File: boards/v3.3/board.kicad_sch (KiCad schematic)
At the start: 50 parts, among them J1 KF301-2P, J2 KF301-2P, J3 KF301-2P, J4 KF301-2P, J5 KF301-2P, J6 KF301-2P, P1 Pin Header, P2 Pin Header, P3 Pin Header, P4 Pin Header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

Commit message: The last board and documentation update
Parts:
- added AMP5, AMP6, AMP7, AMP8: TL082, Package_DIP:DIP-8_W7.62mm_Socket, symbol Amplifier_Operational:TL082
- added R13, R14, R15, R16, R17, R18, R19: 1MΩ, Resistor_THT:R_Axial_DIN0207_L6.3mm_D2.5mm_P10.16mm_Horizontal, symbol Device:R
- PS1: value HLK-10M24 -> HLK-5M12
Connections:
- net Current A: now also MCU1.J1_7 (GPIO7), P3.4 (Pin_4), R16.1; no longer AMP2.7, MCU1.J1_6 (GPIO6), P3.1 (Pin_1), R9.1
- net Current B: now also P3.3 (Pin_3), R17.1; no longer AMP3.7, P3.2 (Pin_2), R10.1
- net Current C: now also MCU1.J1_15 (GPIO9), P3.2 (Pin_2), R18.1; no longer AMP4.1, MCU1.J1_16 (GPIO10), P3.3 (Pin_3), R11.1
- net Current N: now also MCU1.J1_16 (GPIO10), P3.1 (Pin_1), R19.1; no longer AMP4.7, MCU1.J1_15 (GPIO9), P3.4 (Pin_4), R12.1
- net GND: now also AMP5.4 (V-), AMP6.4 (V-), AMP7.4 (V-), AMP8.4 (V-)
- net TC A-1: now also AMP5.3 (+), AMP6.3 (+), AMP7.3 (+), AMP8.1, AMP8.2 (-); no longer AMP1.6 (-), AMP1.7, AMP2.5 (+), AMP3.5 (+), AMP4.5 (+)
- net TC A-2: now also AMP4.2 (-); no longer AMP2.6 (-)
- net TC B-2: now also AMP5.2 (-); no longer AMP3.6 (-)
- net TC C-2: now also AMP6.2 (-); no longer AMP4.2 (-)
- net TC N-2: now also AMP7.2 (-); no longer AMP4.6 (-)
- net V1.65: now also AMP8.3 (+); no longer AMP1.5 (+)
- net Vin: now also SW1.2 (B), AMP5.8 (V+), AMP6.8 (V+), AMP7.8 (V+), AMP8.8 (V+); no longer SW1.1 (C)
- net Wave A: now also R13.1; no longer AMP1.1, R6.2
- net Wave B: now also R14.1; no longer AMP2.1, R7.2
- net Wave C: now also MCU1.J1_6 (GPIO6), R15.1; no longer AMP3.1, MCU1.J1_7 (GPIO7), R8.2
- net at PS1.4 (+Vout): now also SW1.3 (A); no longer SW1.2 (B)
- new net: AMP5.1, AMP5.5 (+), R10.1
- new net: AMP3.1, AMP3.5 (+), R8.2
- new net: AMP2.1, AMP2.5 (+), R7.2
- new net: AMP2.6 (-), AMP2.7, R14.2
- new net: AMP6.6 (-), AMP6.7, R18.2
- new net: AMP7.1, AMP7.5 (+), R12.1
- new net: AMP1.6 (-), AMP1.7, R13.2
- new net: AMP1.1, AMP1.5 (+), R6.2
- new net: AMP4.1, AMP4.5 (+), R9.1
- new net: AMP4.6 (-), AMP4.7, R16.2
- new net: AMP6.1, AMP6.5 (+), R11.1
- new net: AMP5.6 (-), AMP5.7, R17.2
- new net: AMP7.6 (-), AMP7.7, R19.2
- new net: AMP3.6 (-), AMP3.7, R15.2
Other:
- note added: "150kΩ"
- note added: "24Ω"
- note added: "3.9Ω"
- note added: "36Ω"
- note added: "3Ω"
- note added: "430Ω"
- note added: "470Ω"
- note added: "5.6Ω"
- note removed: "180kΩ"
- note removed: "27Ω"
- note removed: "3.3Ω"
- note removed: "4.3Ω"
- note removed: "43Ω"
- note removed: "560Ω"
- note removed: "6.8Ω"
- title: Energy Guardian V3.2 Schematic -> Energy Guardian V3.3 Schematic
- moved on the sheet: AMP1C, AMP2C, AMP3C, AMP4C, C1, C2, J1, J2, J3, J4, J5, J6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

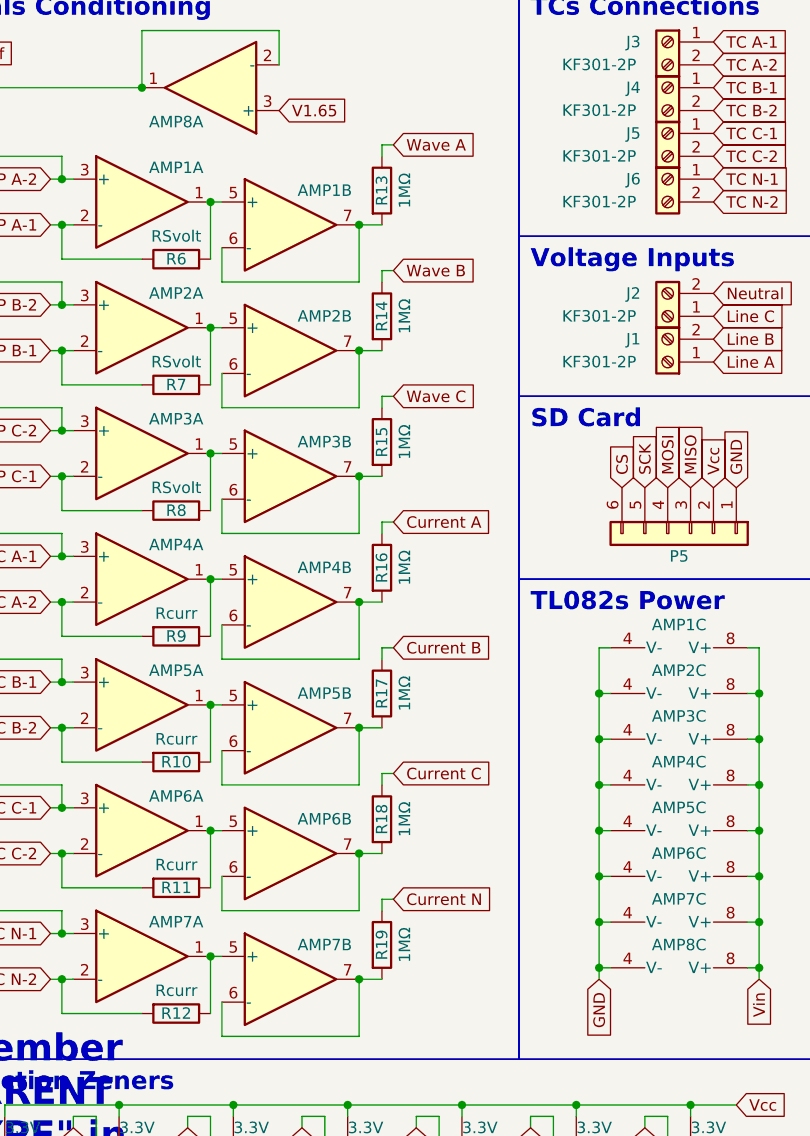
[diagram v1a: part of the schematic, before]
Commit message: Update the list of components and calcs
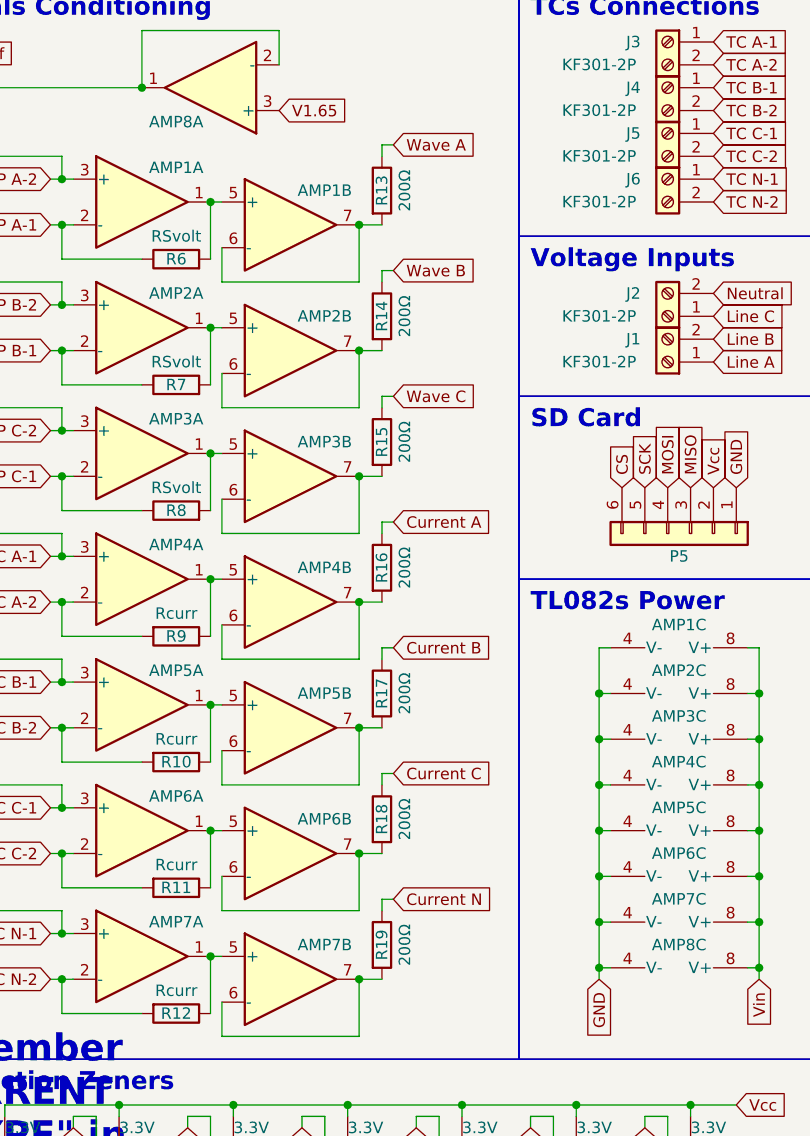
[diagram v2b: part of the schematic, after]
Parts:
- R13, R14, R15, R16, R17, R18, R19: value 1MΩ -> 200Ω
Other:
- company: https://www.linkedin.com/in/lucasrguerra -> linkedin.com/in/lucasrguerra
- title: Energy Guardian V3.3 Schematic -> Power Vision V3.3 Schematic
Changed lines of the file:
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@@
   (paper "A4")
   (title_block
-    (title "Energy Guardian V3.3 Schematic")
+    (title "Power Vision V3.3 Schematic")
     (date "01/06/2024")
-    (rev "1.1")
-    (company "https://www.linkedin.com/in/lucasrguerra")
+    (rev "1.2")
+    (company "linkedin.com/in/lucasrguerra")
+    (comment 1 "github.com/lucasrguerra/power_vision")
   )
   (junction (at 179.07 148.59) (diameter 0) (color 0 0 0 0)
@@
       (effects (font (size 1.27 1.27)))
     )
-    (property "Value" "1MΩ" (at 160.02 106.68 90)
+    (property "Value" "200Ω" (at 160.02 106.68 90)
       (effects (font (size 1.27 1.27)))
     )
@@
       (effects (font (size 1.27 1.27)))
     )
-    (property "Value" "1MΩ" (at 160.02 36.83 90)
+    (property "Value" "200Ω" (at 160.02 36.83 90)
       (effects (font (size 1.27 1.27)))
     )
@@
       (effects (font (size 1.27 1.27)))
     )
-    (property "Value" "1MΩ" (at 160.02 78.74 90)
+    (property "Value" "200Ω" (at 160.02 78.74 90)
       (effects (font (size 1.27 1.27)))
     )
@@
       (effects (font (size 1.27 1.27)))
     )
-    (property "Value" "1MΩ" (at 160.02 50.8 90)
+    (property "Value" "200Ω" (at 160.02 50.8 90)
       (effects (font (size 1.27 1.27)))
     )
@@
       (effects (font (size 1.27 1.27)))
     )
-    (property "Value" "1MΩ" (at 160.02 92.71 90)
+    (property "Value" "200Ω" (at 160.02 92.71 90)
       (effects (font (size 1.27 1.27)))
     )
@@
       (effects (font (size 1.27 1.27)))
     )
-    (property "Value" "1MΩ" (at 160.02 120.65 90)
+    (property "Value" "200Ω" (at 160.02 120.65 90)
       (effects (font (size 1.27 1.27)))
     )
@@
       (effects (font (size 1.27 1.27)))
     )
-    (property "Value" "1MΩ" (at 160.02 64.77 90)
+    (property "Value" "200Ω" (at 160.02 64.77 90)
       (effects (font (size 1.27 1.27)))
     )

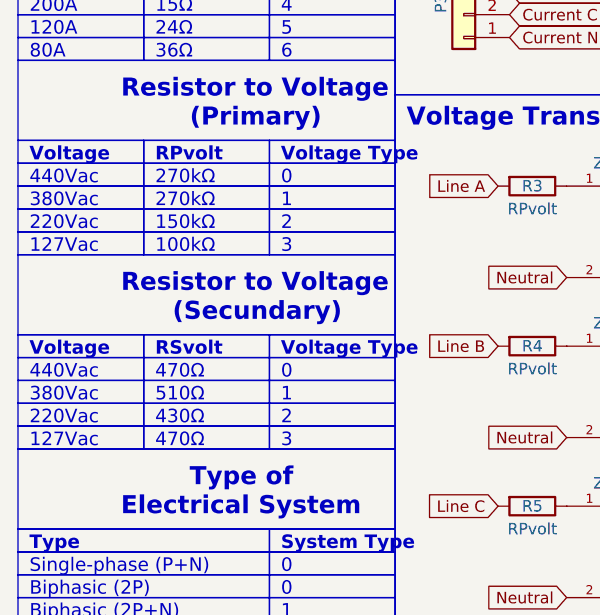
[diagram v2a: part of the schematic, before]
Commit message: Add the earth plan in the v3.3 board
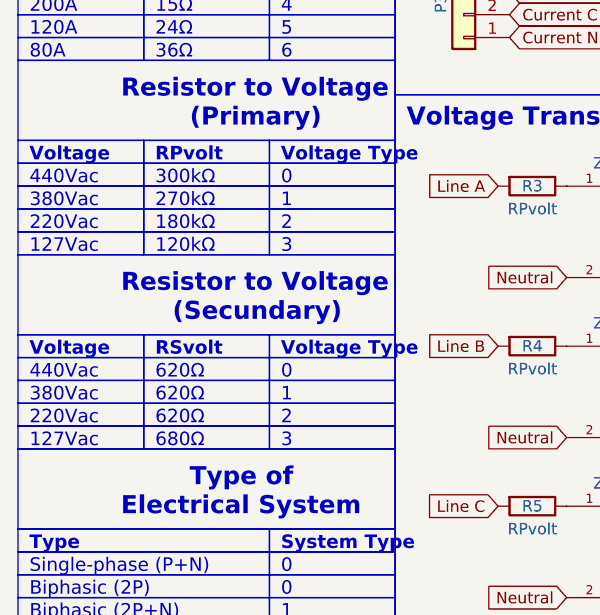
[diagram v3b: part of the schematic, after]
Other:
- note added: "120kΩ"
- note added: "180kΩ"
- note added: "300kΩ"
- note added: "620Ω"
- note added: "680Ω"
- note removed: "100kΩ"
- note removed: "150kΩ"
- note removed: "430Ω"
- note removed: "470Ω"
- note removed: "510Ω"
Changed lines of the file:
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@@
   (title_block
     (title "Power Vision V3.3 Schematic")
-    (date "01/06/2024")
-    (rev "1.2")
+    (date "02/06/2024")
+    (rev "1.3")
     (company "linkedin.com/in/lucasrguerra")
     (comment 1 "github.com/lucasrguerra/power_vision")
@@
     (effects (font (face "Calibri") (size 1.5 1.5)) (justify left bottom))
   )
-  (text "510Ω" (at 29.21 81.28 0)
+  (text "620Ω" (at 29.21 81.28 0)
     (effects (font (face "Calibri") (size 1.5 1.5)) (justify left bottom))
   )
@@
     (effects (font (face "Calibri") (size 2 2) (thickness 0.254) bold) (justify left bottom))
   )
-  (text "270kΩ" (at 29.21 57.15 0)
+  (text "300kΩ" (at 29.21 57.15 0)
     (effects (font (face "Calibri") (size 1.5 1.5)) (justify left bottom))
   )
@@
     (effects (font (face "Calibri") (size 1.5 1.5)) (justify left bottom))
   )
-  (text "100kΩ" (at 29.21 64.77 0)
+  (text "120kΩ" (at 29.21 64.77 0)
     (effects (font (face "Calibri") (size 1.5 1.5)) (justify left bottom))
   )
@@
     (effects (font (face "Calibri") (size 1.5 1.5)) (justify left bottom))
   )
-  (text "430Ω" (at 29.21 83.82 0)
+  (text "620Ω" (at 29.21 83.82 0)
     (effects (font (face "Calibri") (size 1.5 1.5)) (justify left bottom))
   )
@@
     (effects (font (face "Calibri") (size 1.5 1.5)) (justify left bottom))
   )
-  (text "150kΩ" (at 29.21 62.23 0)
+  (text "180kΩ" (at 29.21 62.23 0)
     (effects (font (face "Calibri") (size 1.5 1.5)) (justify left bottom))
   )
@@
     (effects (font (face "Calibri") (size 1.5 1.5)) (justify left bottom))
   )
-  (text "470Ω" (at 29.21 86.36 0)
+  (text "680Ω" (at 29.21 86.36 0)
     (effects (font (face "Calibri") (size 1.5 1.5)) (justify left bottom))
   )
@@
     (effects (font (face "Calibri") (size 1.5 1.5)) (justify left bottom))
   )
-  (text "470Ω" (at 29.21 78.74 0)
-    (effects (font (face "Calibri") (size 1.5 1.5)) (justify left bottom))
-  )
+  (text "620Ω" (at 29.21 78.74 0)
+    (effects (font (face "Calibri") (size 1.5 1.5)) (justify left bottom))
+  )
